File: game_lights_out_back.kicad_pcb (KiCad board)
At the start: 2 copper layers, 171 x 127.3 mm, 5 parts

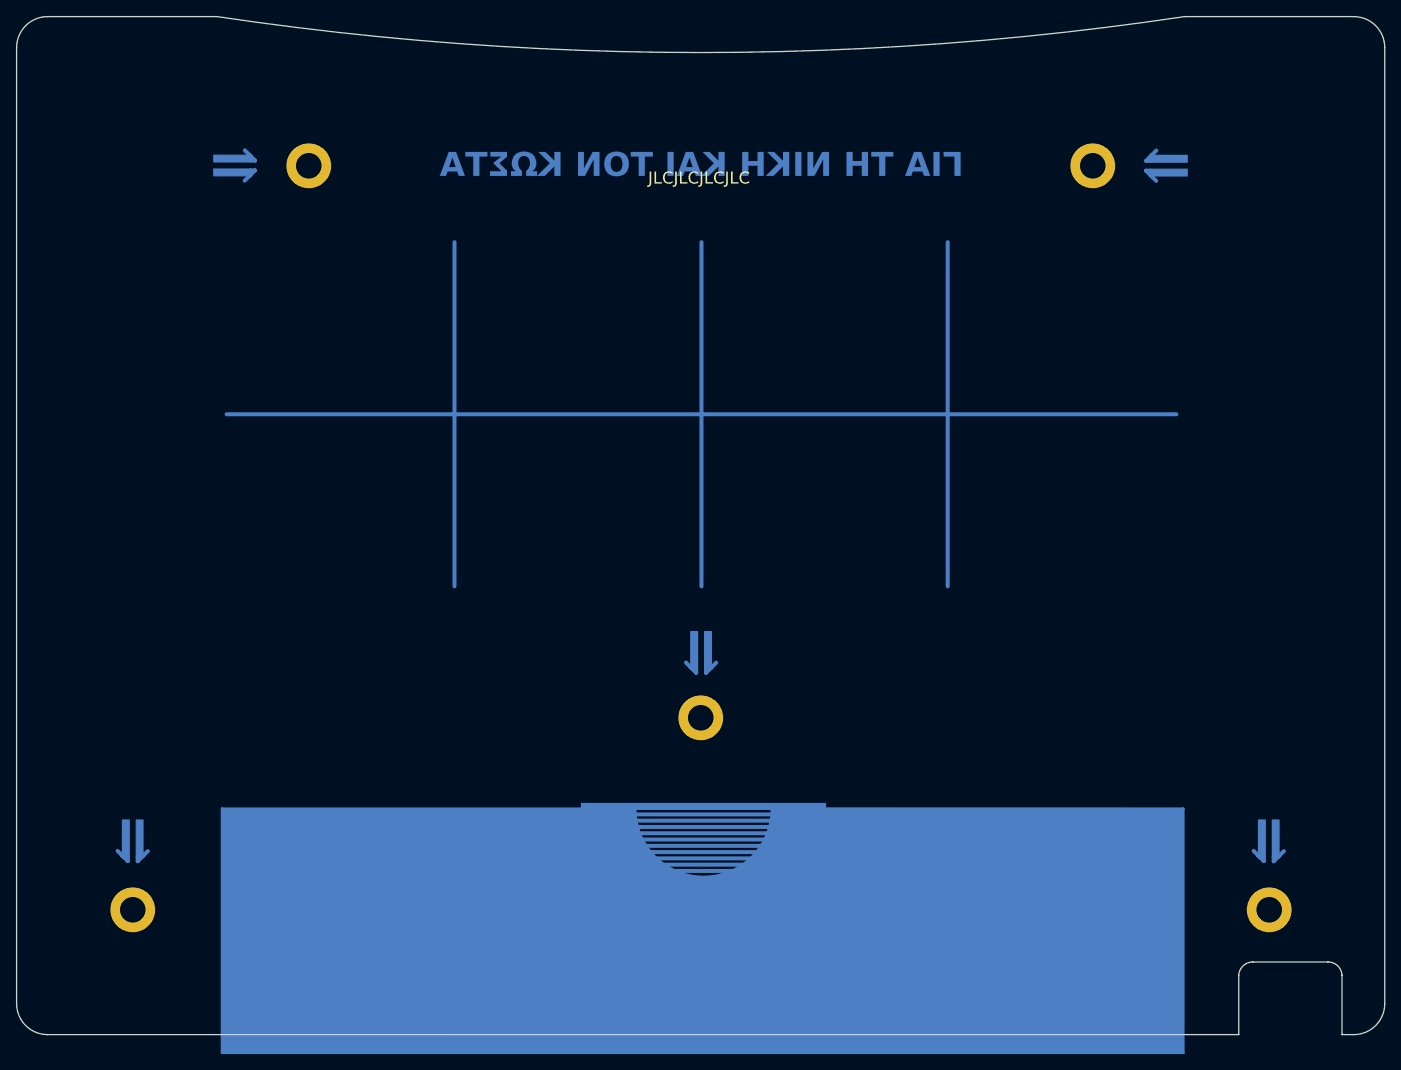
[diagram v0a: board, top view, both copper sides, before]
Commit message: Redesign to match the updated main board
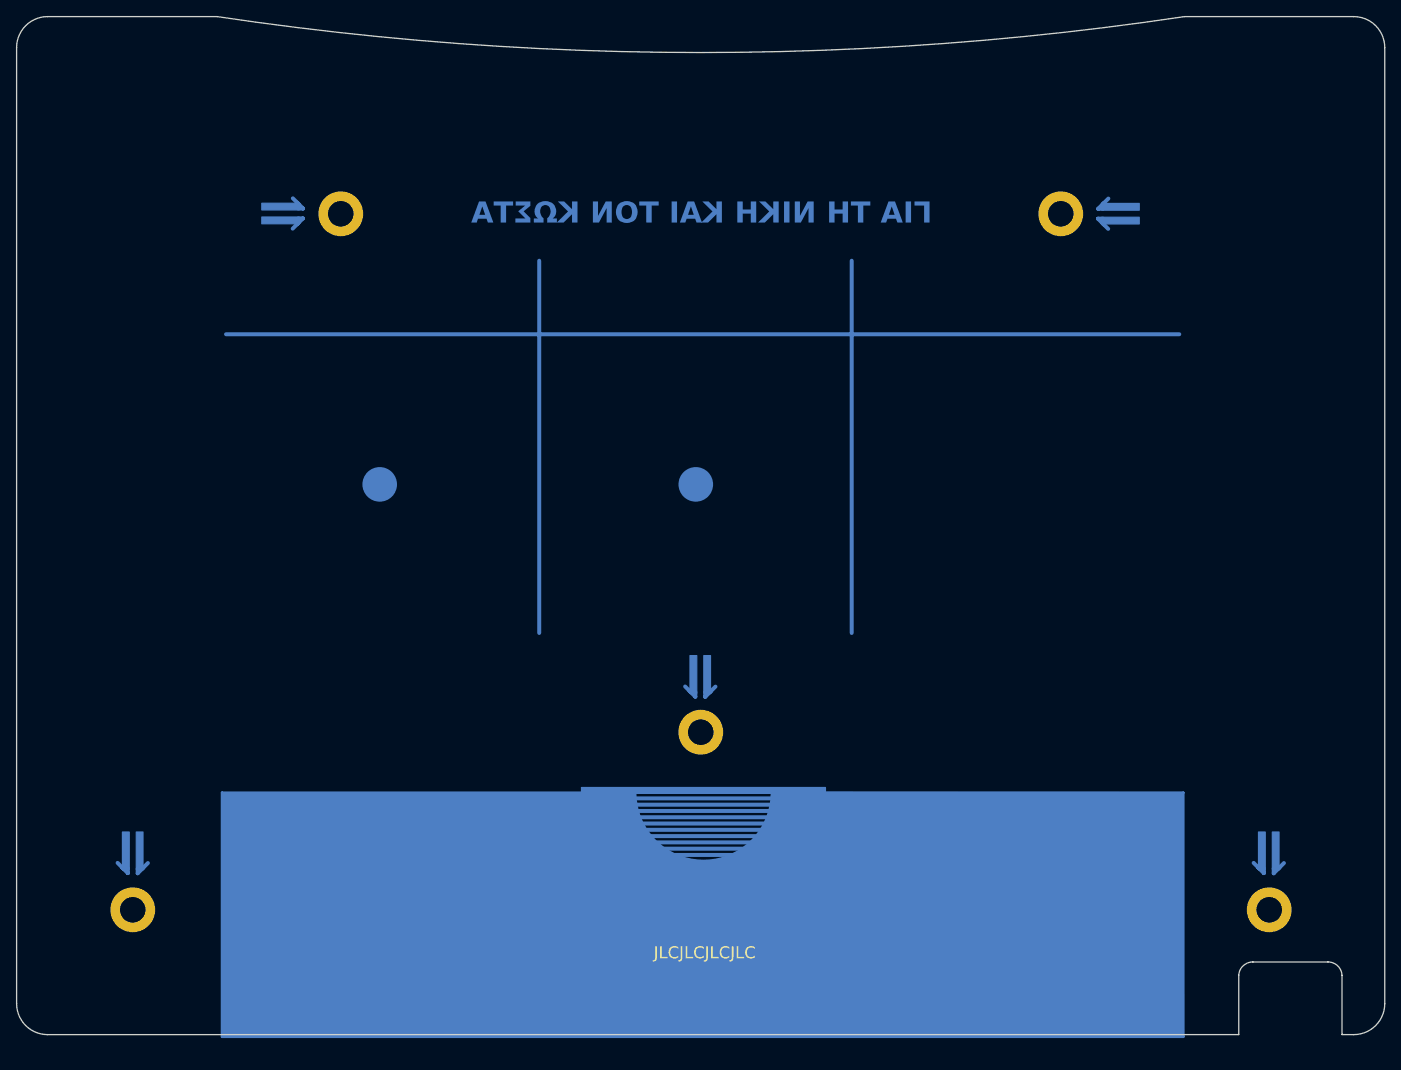
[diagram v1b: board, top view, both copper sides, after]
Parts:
- moved REF** 7.21 mm to (68.0, 61.0)
- moved REF** 7.21 mm to (158.0, 61.0)
- moved REF** 1.80 mm to (113.0, 125.8)
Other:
- board text added: "///"
- board text added: "Every configuration is solvable. Don't blame the game ;)"
- board text added: "Fun facts:"
- board text added: "Marked lights will toggle when the middle one is pressed."
- board text added: "No key needs to be pressed more than once. It won't make any difference."
- board text removed: "MAD"

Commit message: Minor aesthetic changes
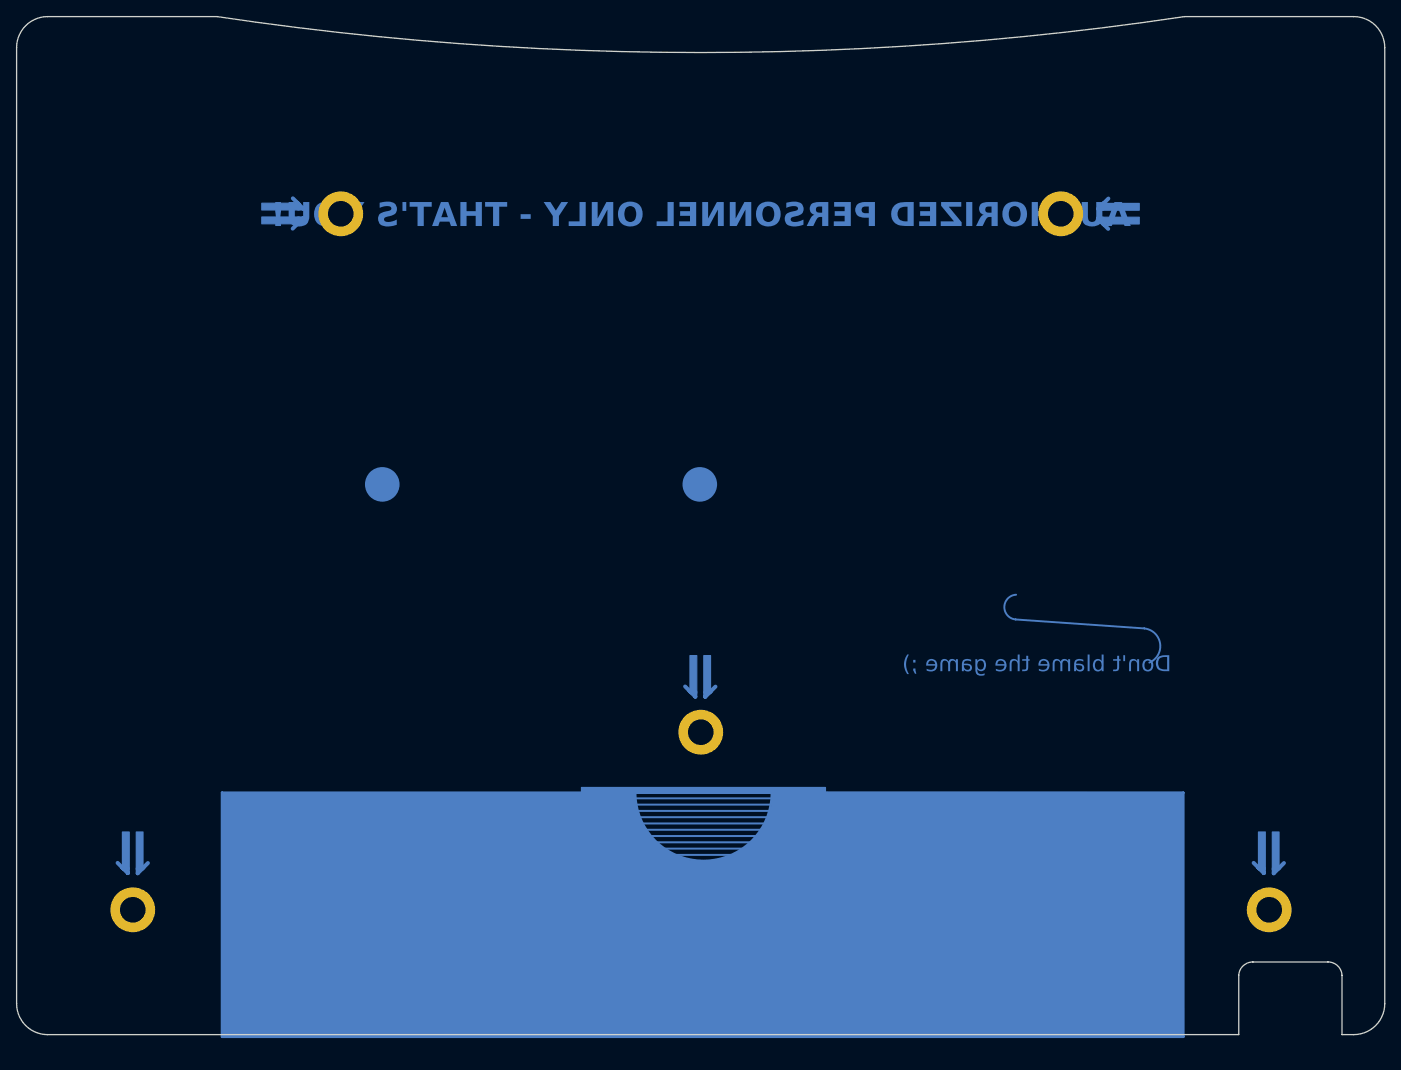
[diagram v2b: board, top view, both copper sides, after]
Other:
- board text added: "* All possible configurations are solvable."
- board text added: "* No button needs to be pressed more than once!"
- board text added: "AUTHORIZED PERSONNEL ONLY - THAT'S YOU!"
- board text added: "Don't blame the game ;)"
- board text added: "Pressing a button toggles the designated surrounding lights."
- board text removed: "Every configuration is solvable. Don't blame the game ;)"
- board text removed: "JLCJLCJLCJLC"
- board text removed: "Marked lights will toggle when the middle one is pressed."
- board text removed: "No key needs to be pressed more than once. It won't make any difference."
- board text removed: "ΓΙΑ ΤΗ ΝΙΚΗ ΚΑΙ ΤΟΝ ΚΩΣΤΑ"
